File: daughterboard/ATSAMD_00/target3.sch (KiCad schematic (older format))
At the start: 22 parts, among them U3 ATSAMD21E16L-AFT

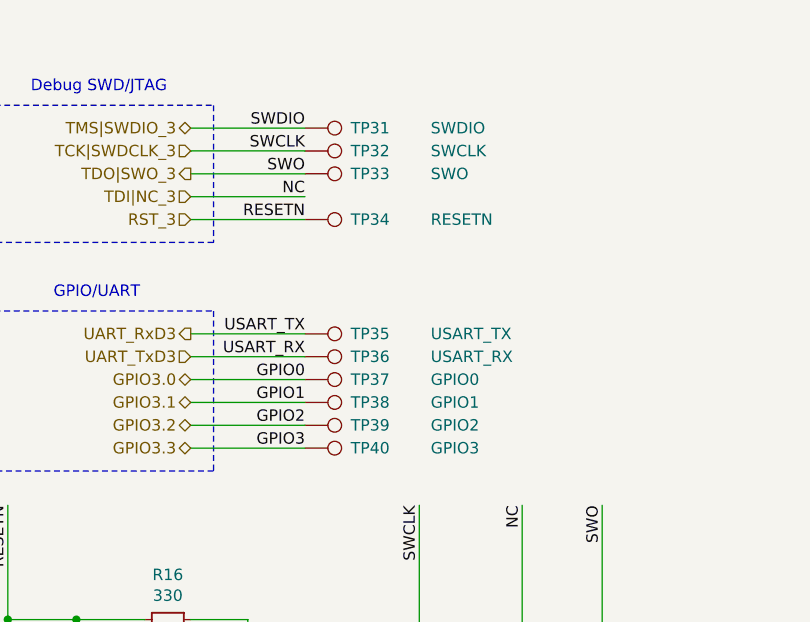
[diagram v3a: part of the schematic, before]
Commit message: finished ATSAMD daughterboard layout
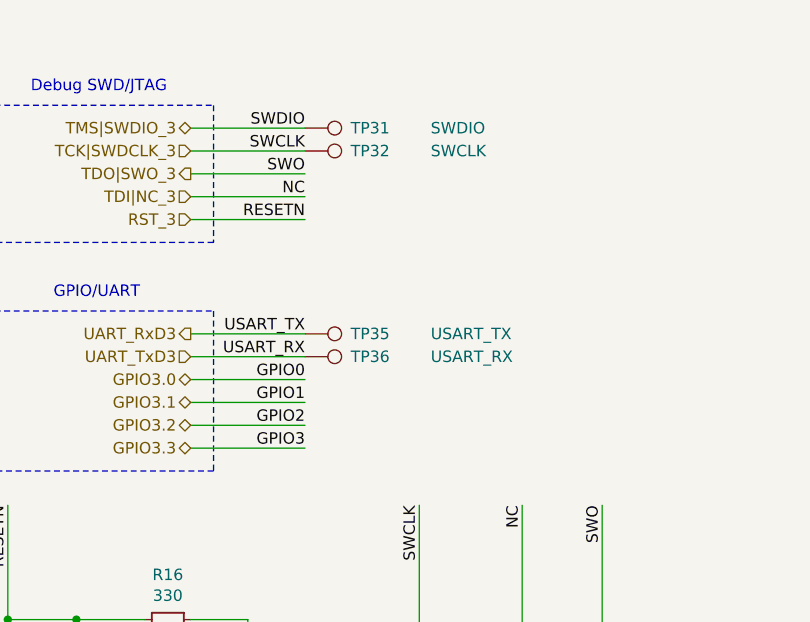
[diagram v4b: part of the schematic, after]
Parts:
- removed TP33: SWO, symbol Connector:TestPoint
- removed TP34: RESETN, symbol Connector:TestPoint
- removed TP37: GPIO0, symbol Connector:TestPoint
- removed TP38: GPIO1, symbol Connector:TestPoint
- removed TP39: GPIO2, symbol Connector:TestPoint
- removed TP40: GPIO3, symbol Connector:TestPoint
- C15, C16, C17, C18, C19: footprint (none) -> Capacitor_SMD:C_0603_1608Metric_Pad1.05x0.95mm_HandSolder
- JP4: footprint (none) -> Jumper:SolderJumper-2_P1.3mm_Open_TrianglePad1.0x1.5mm
- R15, R16, R17, R18, R19: footprint (none) -> Resistor_SMD:R_0603_1608Metric_Pad1.05x0.95mm_HandSolder
- TP31, TP32, TP35, TP36: footprint (none) -> TestPoint:TestPoint_Pad_1.0x1.0mm
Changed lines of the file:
@@
 F 0 "C17" H 7542 2146 50  0000 L CNN
 F 1 "10u" H 7542 2055 50  0000 L CNN
-F 2 "" H 7450 2100 50  0001 C CNN
+F 2 "Capacitor_SMD:C_0603_1608Metric_Pad1.05x0.95mm_HandSolder" H 7450 2100 50  0001 C CNN
 F 3 "~" H 7450 2100 50  0001 C CNN
 	1    7450 2100
@@
 F 0 "C16" H 6242 2146 50  0000 L CNN
 F 1 "1u" H 6242 2055 50  0000 L CNN
-F 2 "" H 6150 2100 50  0001 C CNN
+F 2 "Capacitor_SMD:C_0603_1608Metric_Pad1.05x0.95mm_HandSolder" H 6150 2100 50  0001 C CNN
 F 3 "~" H 6150 2100 50  0001 C CNN
 	1    6150 2100
@@
 F 0 "C18" H 7942 2146 50  0000 L CNN
 F 1 "100n" H 7942 2055 50  0000 L CNN
-F 2 "" H 7850 2100 50  0001 C CNN
+F 2 "Capacitor_SMD:C_0603_1608Metric_Pad1.05x0.95mm_HandSolder" H 7850 2100 50  0001 C CNN
 F 3 "~" H 7850 2100 50  0001 C CNN
 	1    7850 2100
@@
 F 0 "C19" H 8342 2146 50  0000 L CNN
 F 1 "100n" H 8342 2055 50  0000 L CNN
-F 2 "" H 8250 2100 50  0001 C CNN
+F 2 "Capacitor_SMD:C_0603_1608Metric_Pad1.05x0.95mm_HandSolder" H 8250 2100 50  0001 C CNN
 F 3 "~" H 8250 2100 50  0001 C CNN
 	1    8250 2100
@@
 F 0 "R15" H 909 4346 50  0000 L CNN
 F 1 "10k" H 909 4255 50  0000 L CNN
-F 2 "" H 850 4300 50  0001 C CNN
+F 2 "Resistor_SMD:R_0603_1608Metric_Pad1.05x0.95mm_HandSolder" H 850 4300 50  0001 C CNN
 F 3 "~" H 850 4300 50  0001 C CNN
 	1    850  4300
@@
 F 0 "R16" V 1354 3850 50  0000 C CNN
 F 1 "330" V 1445 3850 50  0000 C CNN
-F 2 "" H 1550 3850 50  0001 C CNN
+F 2 "Resistor_SMD:R_0603_1608Metric_Pad1.05x0.95mm_HandSolder" H 1550 3850 50  0001 C CNN
 F 3 "~" H 1550 3850 50  0001 C CNN
 	1    1550 3850
@@
 F 0 "C15" H 1242 4346 50  0000 L CNN
 F 1 "100n" H 1242 4255 50  0000 L CNN
-F 2 "" H 1150 4300 50  0001 C CNN
+F 2 "Capacitor_SMD:C_0603_1608Metric_Pad1.05x0.95mm_HandSolder" H 1150 4300 50  0001 C CNN
 F 3 "~" H 1150 4300 50  0001 C CNN
 	1    1150 4300
@@
 F 0 "JP4" V 1946 4212 50  0000 R CNN
 F 1 "NRST" V 1855 4212 50  0000 R CNN
-F 2 "" H 1900 4300 50  0001 C CNN
+F 2 "Jumper:SolderJumper-2_P1.3mm_Open_TrianglePad1.0x1.5mm" H 1900 4300 50  0001 C CNN
 F 3 "~" H 1900 4300 50  0001 C CNN
 	1    1900 4300
@@
 F 0 "R17" H 2709 4296 50  0000 L CNN
 F 1 "1k" H 2709 4205 50  0000 L CNN
-F 2 "" H 2650 4250 50  0001 C CNN
+F 2 "Resistor_SMD:R_0603_1608Metric_Pad1.05x0.95mm_HandSolder" H 2650 4250 50  0001 C CNN
 F 3 "~" H 2650 4250 50  0001 C CNN
 	1    2650 4250
@@
 F 0 "R18" H 3159 4296 50  0000 L CNN
 F 1 "100k" H 3159 4205 50  0000 L CNN
-F 2 "" H 3100 4250 50  0001 C CNN
+F 2 "Resistor_SMD:R_0603_1608Metric_Pad1.05x0.95mm_HandSolder" H 3100 4250 50  0001 C CNN
 F 3 "~" H 3100 4250 50  0001 C CNN
 	1    3100 4250
@@
 F 0 "R19" H 3509 4296 50  0000 L CNN
 F 1 "100k" H 3509 4205 50  0000 L CNN
-F 2 "" H 3450 4250 50  0001 C CNN
+F 2 "Resistor_SMD:R_0603_1608Metric_Pad1.05x0.95mm_HandSolder" H 3450 4250 50  0001 C CNN
 F 3 "~" H 3450 4250 50  0001 C CNN
 	1    3450 4250
@@
 F 0 "TP31" V 2150 1900 50  0000 L CNN
 F 1 "SWDIO" V 2150 2250 50  0000 L CNN
-F 2 "" H 2350 1700 50  0001 C CNN
+F 2 "TestPoint:TestPoint_Pad_1.0x1.0mm" H 2350 1700 50  0001 C CNN
 F 3 "~" H 2350 1700 50  0001 C CNN
 	1    2150 1700
@@
 F 0 "TP32" V 2150 2000 50  0000 L CNN
 F 1 "SWCLK" V 2150 2350 50  0000 L CNN
-F 2 "" H 2350 1800 50  0001 C CNN
+F 2 "TestPoint:TestPoint_Pad_1.0x1.0mm" H 2350 1800 50  0001 C CNN
 F 3 "~" H 2350 1800 50  0001 C CNN
 	1    2150 1800
-	0    1    1    0
-$EndComp
-$Comp
-L Connector:TestPoint TP?
-U 1 1 6191E7D8
-P 2150 1900
-AR Path="/616688D6/6191E7D8" Ref="TP?"  Part="1"
-AR Path="/61668157/6191E7D8" Ref="TP33"  Part="1"
-F 0 "TP33" V 2150 2100 50  0000 L CNN
-F 1 "SWO" V 2150 2450 50  0000 L CNN
-F 2 "" H 2350 1900 50  0001 C CNN
-F 3 "~" H 2350 1900 50  0001 C CNN
-	1    2150 1900
-	0    1    1    0
-$EndComp
-$Comp
-L Connector:TestPoint TP?
-U 1 1 6191E7DE
-P 2150 2100
-AR Path="/616688D6/6191E7DE" Ref="TP?"  Part="1"
-AR Path="/61668157/6191E7DE" Ref="TP34"  Part="1"
-F 0 "TP34" V 2150 2300 50  0000 L CNN
-F 1 "RESETN" V 2150 2650 50  0000 L CNN
-F 2 "" H 2350 2100 50  0001 C CNN
-F 3 "~" H 2350 2100 50  0001 C CNN
-	1    2150 2100
 	0    1    1    0
 $EndComp
@@
 F 0 "TP35" V 2150 2800 50  0000 L CNN
 F 1 "USART_TX" V 2150 3150 50  0000 L CNN
-F 2 "" H 2350 2600 50  0001 C CNN
+F 2 "TestPoint:TestPoint_Pad_1.0x1.0mm" H 2350 2600 50  0001 C CNN
 F 3 "~" H 2350 2600 50  0001 C CNN
 	1    2150 2600
@@
 F 0 "TP36" V 2150 2900 50  0000 L CNN
 F 1 "USART_RX" V 2150 3250 50  0000 L CNN
-F 2 "" H 2350 2700 50  0001 C CNN
+F 2 "TestPoint:TestPoint_Pad_1.0x1.0mm" H 2350 2700 50  0001 C CNN
 F 3 "~" H 2350 2700 50  0001 C CNN
 	1    2150 2700
 	0    1    -1   0
 $EndComp
-$Comp
-L Connector:TestPoint TP?
-U 1 1 6191E7F0
-P 2150 2800
-AR Path="/616688D6/6191E7F0" Ref="TP?"  Part="1"
-AR Path="/61668157/6191E7F0" Ref="TP37"  Part="1"
-F 0 "TP37" V 2150 3000 50  0000 L CNN
-F 1 "GPIO0" V 2150 3350 50  0000 L CNN
-F 2 "" H 2350 2800 50  0001 C CNN
-F 3 "~" H 2350 2800 50  0001 C CNN
-	1    2150 2800
-	0    1    -1   0
-$EndComp
-$Comp
-L Connector:TestPoint TP?
-U 1 1 6191E7F6
-P 2150 2900
-AR Path="/616688D6/6191E7F6" Ref="TP?"  Part="1"
-AR Path="/61668157/6191E7F6" Ref="TP38"  Part="1"
-F 0 "TP38" V 2150 3100 50  0000 L CNN
-F 1 "GPIO1" V 2150 3450 50  0000 L CNN
-F 2 "" H 2350 2900 50  0001 C CNN
-F 3 "~" H 2350 2900 50  0001 C CNN
-	1    2150 2900
-	0    1    -1   0
-$EndComp
-$Comp
-L Connector:TestPoint TP?
-U 1 1 6191E7FC
-P 2150 3000
-AR Path="/616688D6/6191E7FC" Ref="TP?"  Part="1"
-AR Path="/61668157/6191E7FC" Ref="TP39"  Part="1"
-F 0 "TP39" V 2150 3200 50  0000 L CNN
-F 1 "GPIO2" V 2150 3550 50  0000 L CNN
-F 2 "" H 2350 3000 50  0001 C CNN
-F 3 "~" H 2350 3000 50  0001 C CNN
-	1    2150 3000
-	0    1    -1   0
-$EndComp
-$Comp
-L Connector:TestPoint TP?
-U 1 1 6191E802
-P 2150 3100
-AR Path="/616688D6/6191E802" Ref="TP?"  Part="1"
-AR Path="/61668157/6191E802" Ref="TP40"  Part="1"
-F 0 "TP40" V 2150 3300 50  0000 L CNN
-F 1 "GPIO3" V 2150 3650 50  0000 L CNN
-F 2 "" H 2350 3100 50  0001 C CNN
-F 3 "~" H 2350 3100 50  0001 C CNN
-	1    2150 3100
-	0    1    -1   0
-$EndComp
